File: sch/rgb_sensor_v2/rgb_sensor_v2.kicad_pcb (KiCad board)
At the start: 2 copper layers, 57 parts, among them J1 Conn_01x20_Male, Q1 2N7002, Q2 2N7002, Q3 2N7002, Q4 2N7002, Q5 2N7002, U1 TCS34725FN, U2 TCS34725FN, U3 TCS34725FN, U4 TCS34725FN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

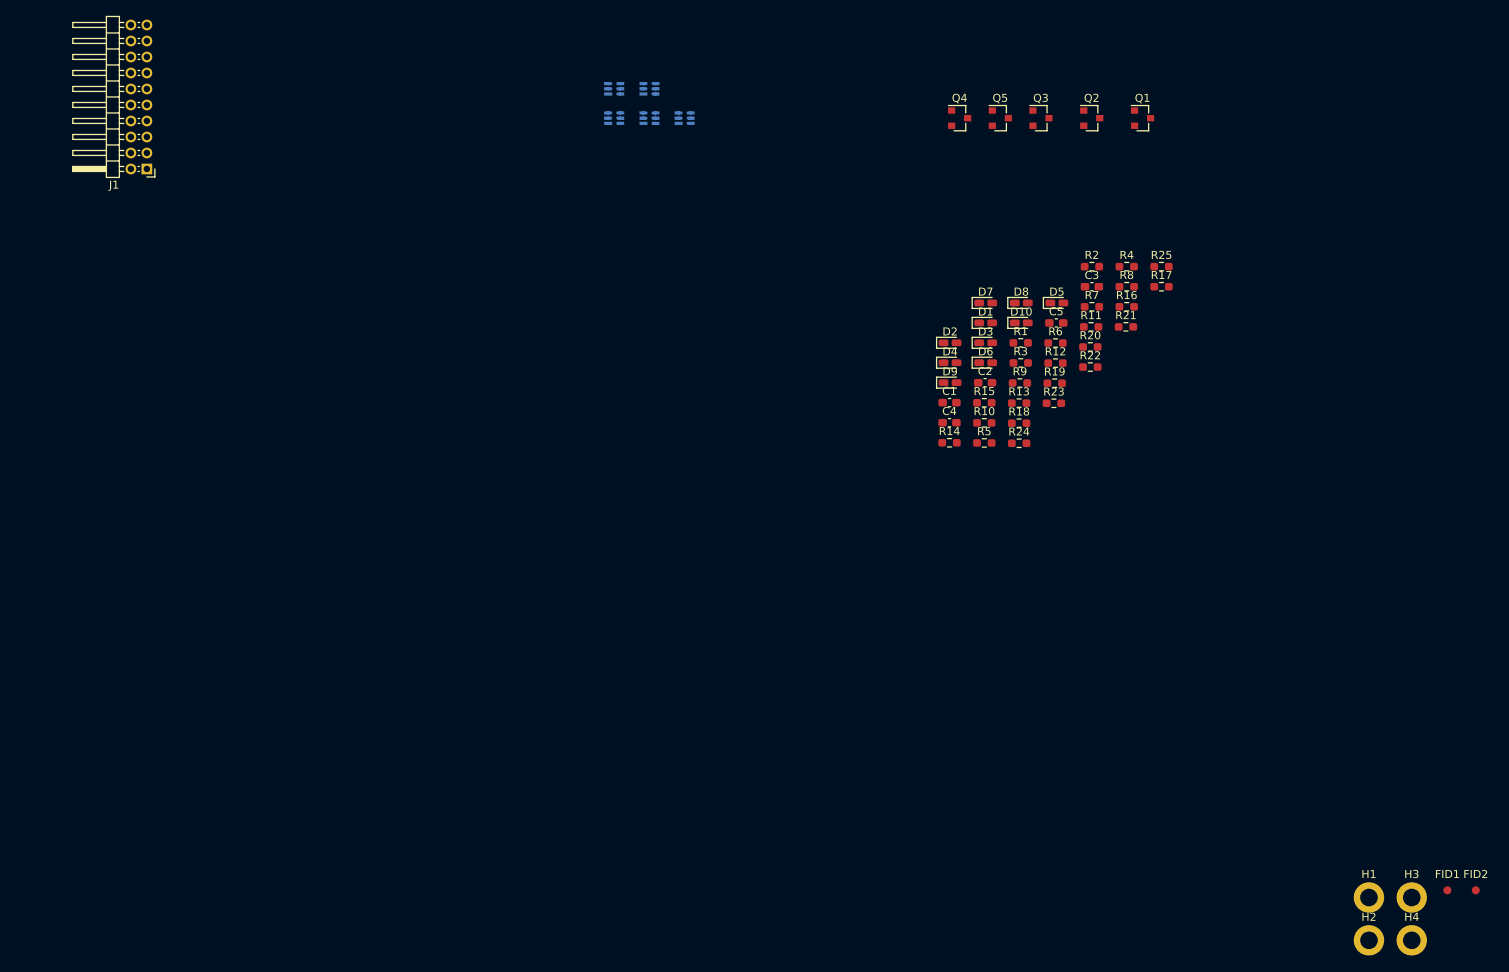
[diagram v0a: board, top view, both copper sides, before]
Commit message: some layout done
beefore changing pin assignment on main connector
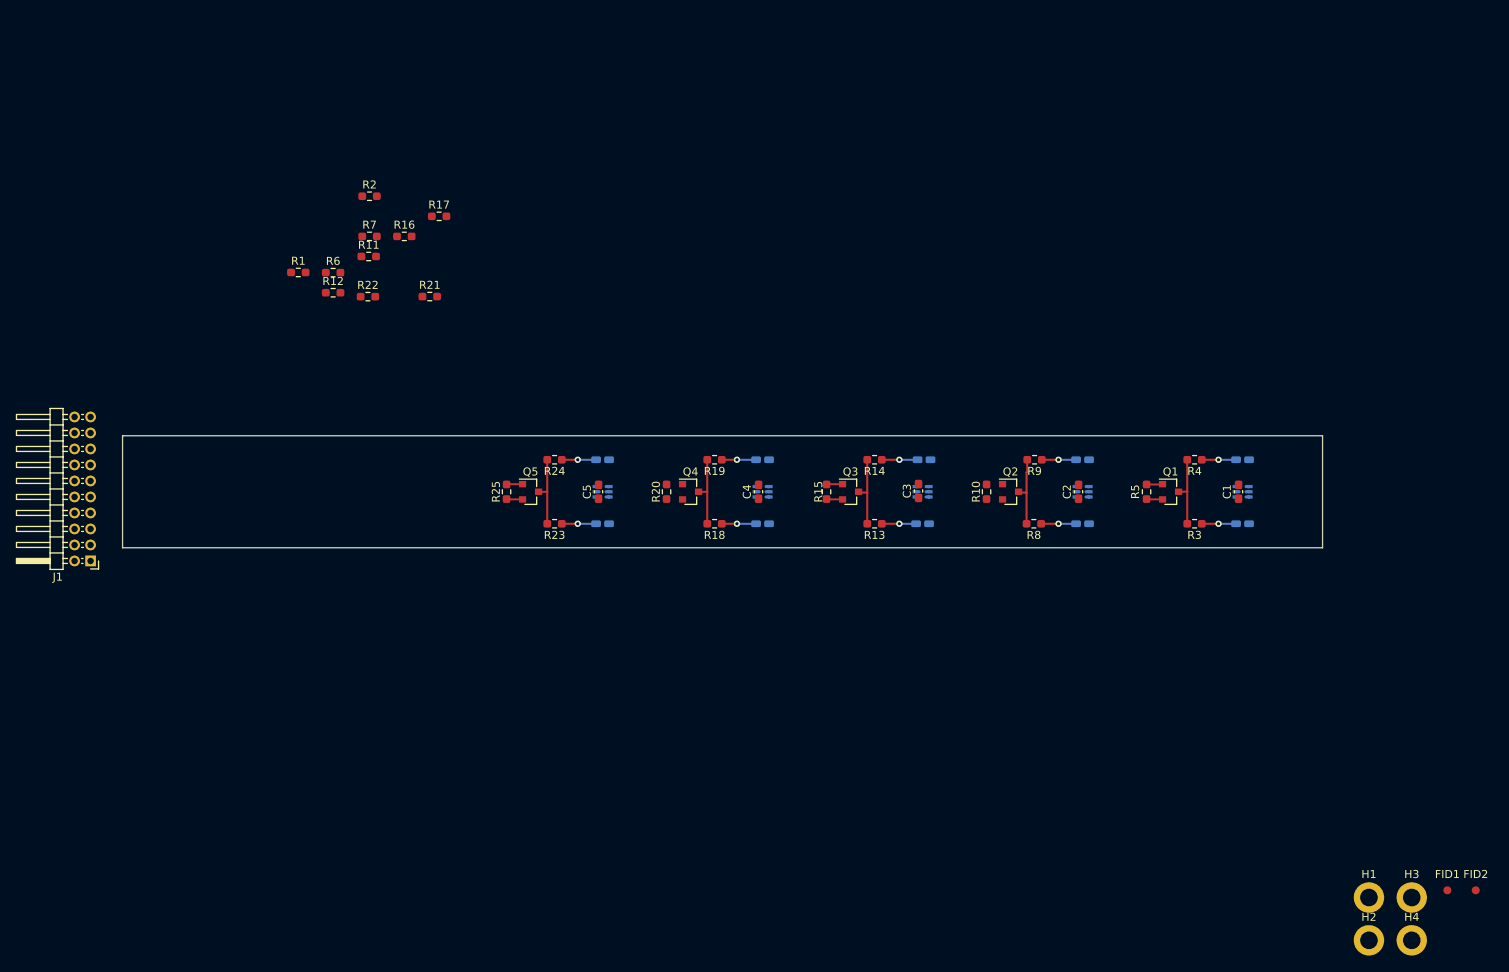
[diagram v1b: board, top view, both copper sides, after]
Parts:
- D1, D10, D2, D3, D4, D5, D6, D7, D8, D9: moved to B.Cu
- moved U1 91.4 mm to (228.4, 97.5)
- moved R12 90.7 mm to (114.7, 72.6)
- moved R17 90.7 mm to (128.0, 63.1)
- moved R22 90.7 mm to (119.1, 73.1)
- moved R6 90.7 mm to (114.7, 70.1)
- moved R11 90.7 mm to (119.2, 68.1)
- moved R2 90.7 mm to (119.3, 60.6)
- moved R7 90.7 mm to (119.3, 65.6)
- moved R1 90.7 mm to (110.4, 70.1)
- moved R16 90.7 mm to (123.6, 65.6)
- moved R21 87.1 mm to (126.8, 73.1)
- moved R25 86.6 mm to (136.4, 97.5), turned to 270 degrees
- moved U2 77.2 mm to (208.4, 97.5)
- moved Q5 75.0 mm to (139.4, 97.5)
- moved R23 64.2 mm to (142.4, 101.5), turned to 180 degrees
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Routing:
- net Net-(Q3-Pad3): track 0.00 -> 9.13 mm
- net Net-(Q5-Pad3): track 0.00 -> 9.09 mm
- net Net-(Q4-Pad3): track 0.00 -> 9.09 mm
- net Net-(Q1-Pad3): track 0.00 -> 9.09 mm
- net Net-(Q2-Pad3): track 0.00 -> 9.08 mm
- net GND: track 0.00 -> 6.05 mm
- net Net-(D6-Pad1): track 0.00 -> 4.46 mm, vias 0 -> 1
- net Net-(D3-Pad1): track 0.00 -> 4.36 mm, vias 0 -> 1
- net Net-(D9-Pad1): track 0.00 -> 4.28 mm, vias 0 -> 1
- net Net-(D8-Pad1): track 0.00 -> 4.28 mm, vias 0 -> 1
- net Net-(D7-Pad1): track 0.00 -> 4.28 mm, vias 0 -> 1
- net Net-(D5-Pad1): track 0.00 -> 4.28 mm, vias 0 -> 1
- net Net-(D4-Pad1): track 0.00 -> 4.28 mm, vias 0 -> 1
- net Net-(D2-Pad1): track 0.00 -> 4.28 mm, vias 0 -> 1
- net Net-(D10-Pad1): track 0.00 -> 4.28 mm, vias 0 -> 1
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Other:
- board outline added: 150 x 14 mm
- board text added: "Desk"

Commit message: zrobiony routing ścieżek
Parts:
- moved H1 54.9 mm to (234.9, 94.1)
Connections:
- J1 pad 10: SDA3 -> SDA2
- J1 pad 11: LED3 -> LED2
- J1 pad 12: SCL4 -> SCL3
- J1 pad 13: SDA4 -> SDA3
- J1 pad 14: LED4 -> LED3
- J1 pad 15: SCL5 -> SCL4
- J1 pad 16: SDA5 -> SDA4
- J1 pad 17: LED5 -> LED4
- J1 pad 18: GND -> SCL5
- J1 pad 19: GND -> SDA5
- J1 pad 20: GND -> LED5
- J1 pad 3: SCL1 -> GND
- J1 pad 4: SDA1 -> GND
- J1 pad 5: LED1 -> GND
- J1 pad 6: SCL2 -> SCL1
- J1 pad 7: SDA2 -> SDA1
- J1 pad 8: LED2 -> LED1
- J1 pad 9: SCL3 -> SCL2
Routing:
- net +3V3: track 0.00 -> 152.3 mm, vias 0 -> 5
- net SDA1: track 0.00 -> 137.0 mm
- net SCL1: track 0.00 -> 131.8 mm
- net LED1: track 2.02 -> 120.2 mm, vias 0 -> 1
- net SDA2: track 0.00 -> 116.0 mm
- net SCL2: track 0.00 -> 111.4 mm
- net LED2: track 0.00 -> 100.5 mm, vias 0 -> 1
- net SDA3: track 0.00 -> 95.0 mm
- net SCL3: track 0.00 -> 88.5 mm
- net SDA4: track 0.00 -> 74.9 mm
- net LED3: track 2.02 -> 76.8 mm, vias 0 -> 1
- net SCL4: track 0.00 -> 67.8 mm
- net LED4: track 0.00 -> 61.4 mm, vias 0 -> 1
- net SDA5: track 0.00 -> 51.3 mm
- net SCL5: track 0.00 -> 45.4 mm
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
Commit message: Zapisany postęp godzinowy
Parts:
- moved R1 116.5 mm to (223.6, 97.5), turned to 90 degrees
- moved R2 112.1 mm to (225.1, 97.5), turned to 90 degrees
- moved R6 93.1 mm to (203.7, 97.5), turned to 90 degrees
- moved R7 91.7 mm to (205.2, 97.5), turned to 90 degrees
- moved R12 65.7 mm to (180.1, 78.9)
- moved R11 61.3 mm to (180.0, 75.8)
- moved H2 52.8 mm to (235.4, 101.5)
- moved J1 4.05 mm to (88.4, 105.5)
- moved H1 0.78 mm to (235.4, 93.5)
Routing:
- net +3V3: track 152.3 -> 230.1 mm, vias 5 -> 13
- net SDA2: track 116.0 -> 118.8 mm, vias 0 -> 1
- net SDA1: track 137.0 -> 139.5 mm, vias 0 -> 1
- net SCL1: track 131.8 -> 133.7 mm, vias 0 -> 1
- net SCL2: track 111.4 -> 113.1 mm, vias 0 -> 1
- added copper zone on F.Cu, net GND

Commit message: Pullus routed
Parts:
- moved R16 51.5 mm to (164.0, 97.5), turned to 90 degrees
- moved R17 50.9 mm to (165.5, 97.5), turned to 90 degrees
- moved R22 35.8 mm to (145.3, 97.5), turned to 90 degrees
- moved R21 29.7 mm to (143.8, 97.5), turned to 90 degrees
- moved R11 22.0 mm to (183.7, 97.5), turned to 90 degrees
- moved R12 19.3 mm to (185.2, 97.5), turned to 90 degrees
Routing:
- net +3V3: track 230.1 -> 239.5 mm
- net SDA5: track 51.3 -> 57.8 mm, vias 0 -> 1
- net SDA3: track 95.0 -> 97.8 mm, vias 0 -> 1
- net SDA4: track 74.9 -> 76.5 mm, vias 0 -> 1
- net SCL4: track 67.8 -> 69.4 mm, vias 0 -> 1
- net SCL3: track 88.5 -> 90.1 mm, vias 0 -> 1
- net SCL5: track 45.4 -> 46.7 mm, vias 0 -> 1

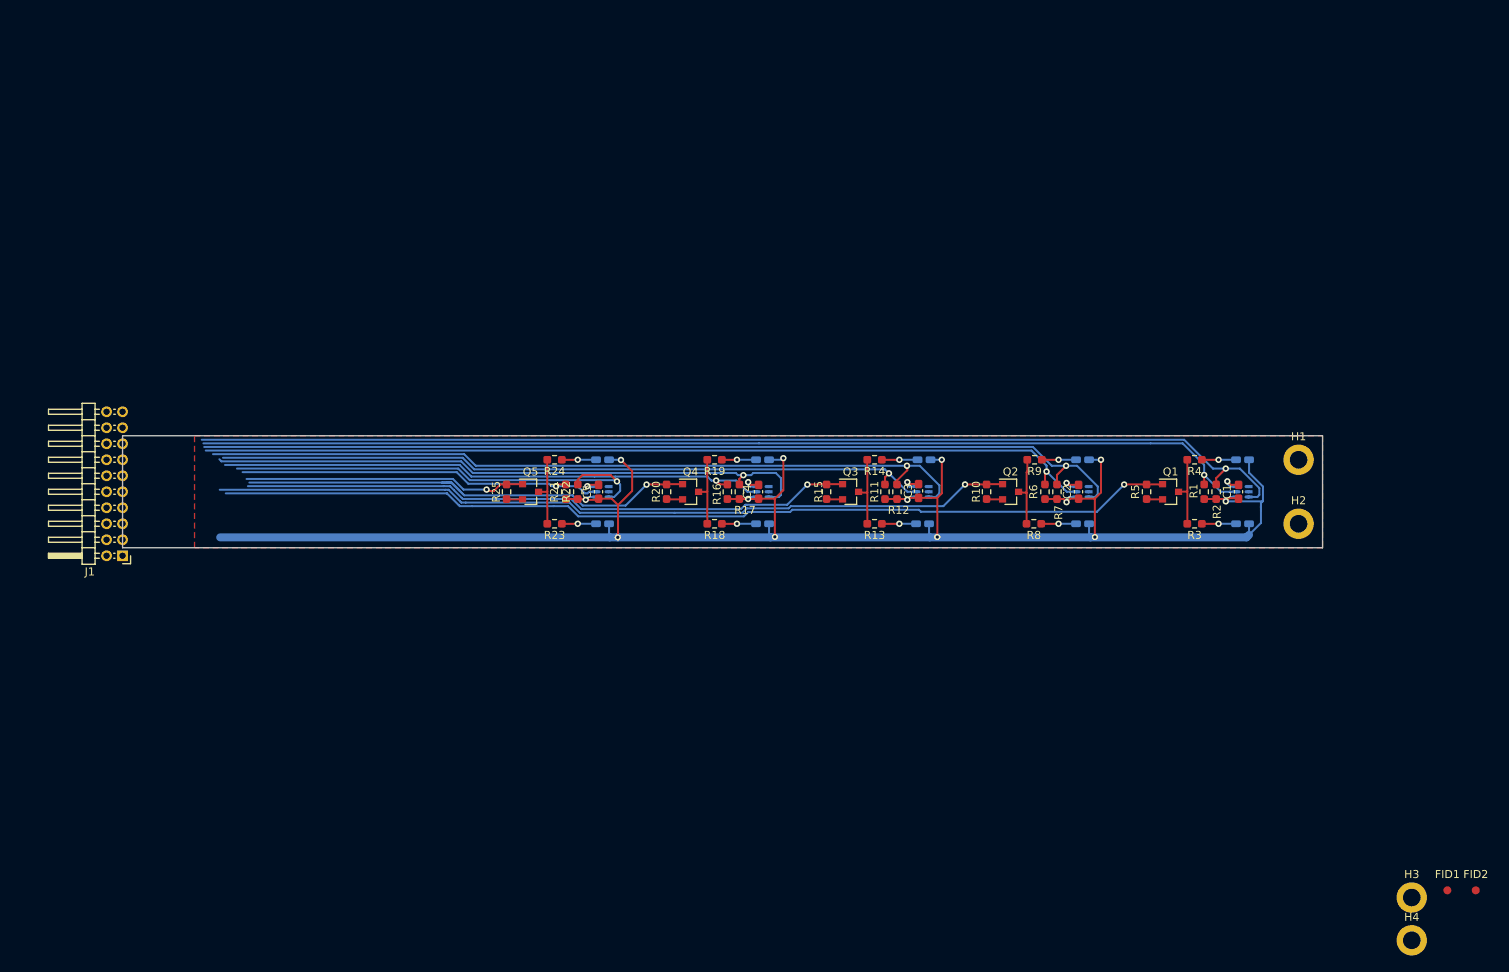
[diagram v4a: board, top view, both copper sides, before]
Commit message: add fab outputs but those are not gerber
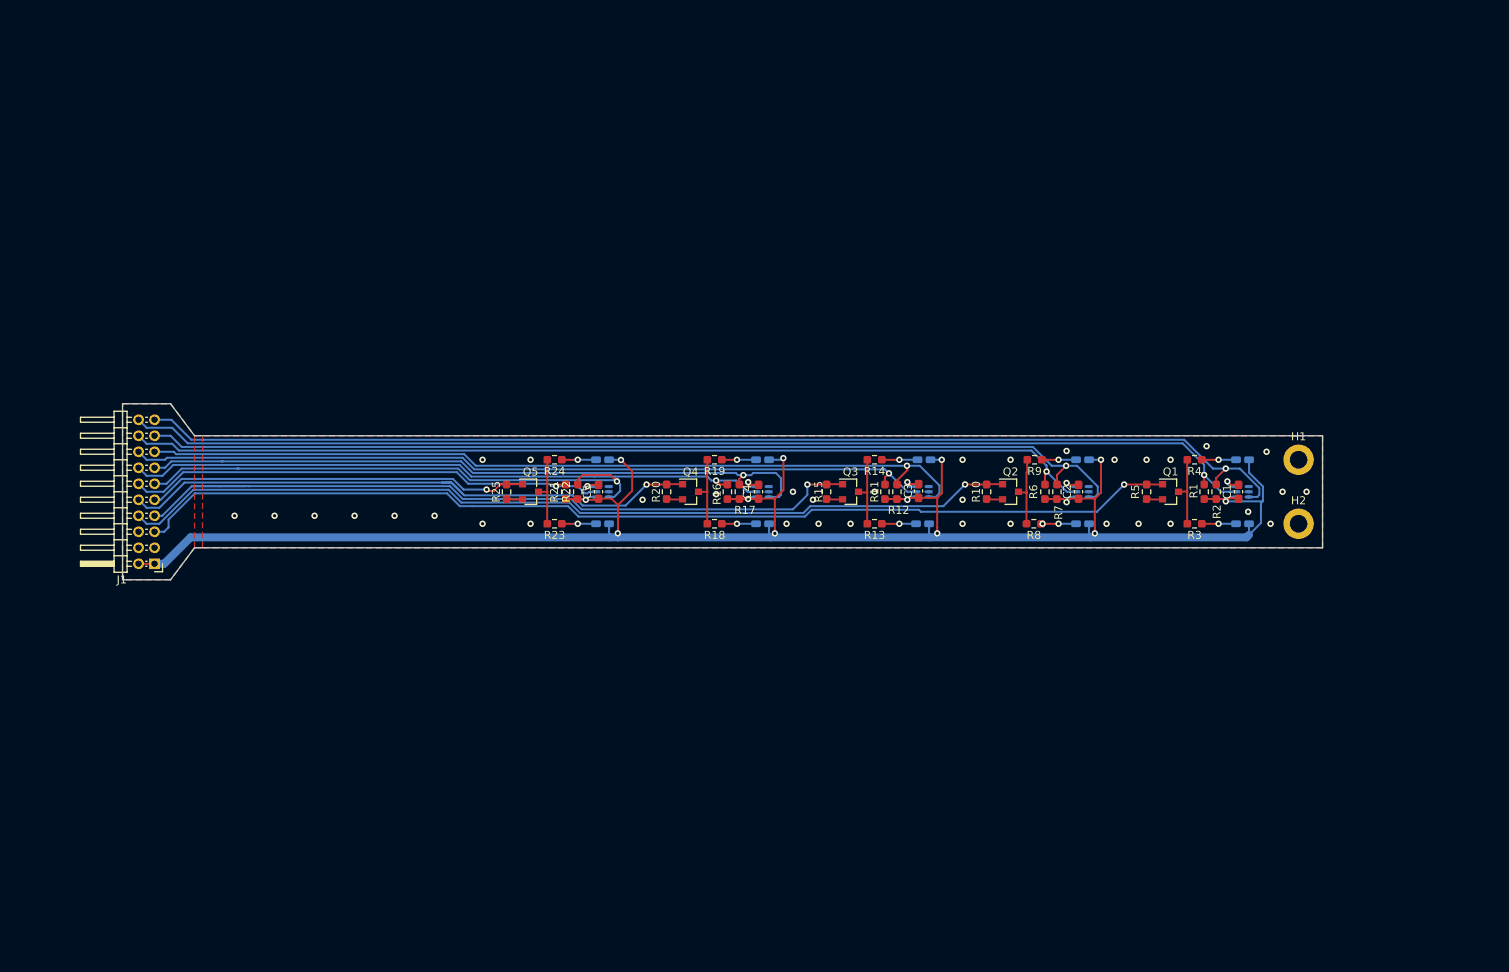
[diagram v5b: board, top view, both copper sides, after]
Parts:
- removed FID1, FID2: Fiducial, Fiducial:Fiducial_1mm_Mask2mm
- removed H3, H4: MountingHole, MountingHole:MountingHole_2.2mm_M2_DIN965_Pad
- moved J1 4.12 mm to (92.4, 106.5)
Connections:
- J1 pad 10: SDA2 -> LED4
- J1 pad 11: LED2 -> SDA5
- J1 pad 12: SCL3 -> SCL5
- J1 pad 13: SDA3 -> SDA4
- J1 pad 14: LED3 -> SCL4
- J1 pad 15: SCL4 -> SDA3
- J1 pad 16: SDA4 -> SCL3
- J1 pad 17: LED4 -> SDA2
- J1 pad 18: SCL5 -> SCL2
- J1 pad 19: SDA5 -> SDA1
- J1 pad 20: LED5 -> SCL1
- J1 pad 5: GND -> LED1
- J1 pad 6: SCL1 -> GND
- J1 pad 7: SDA1 -> LED3
- J1 pad 8: LED1 -> LED2
- J1 pad 9: SCL2 -> LED5
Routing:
- net LED3: track 76.8 -> 98.0 mm
- net LED4: track 61.4 -> 77.0 mm
- net SCL5: track 46.7 -> 61.1 mm
- net LED5: track 35.5 -> 48.1 mm
- net LED2: track 100.5 -> 112.9 mm
- net SCL4: track 69.4 -> 81.5 mm
- net LED1: track 120.2 -> 131.6 mm
- net SDA5: track 57.8 -> 69.1 mm
- net SCL3: track 90.1 -> 101.1 mm
- net SCL1: track 133.7 -> 143.1 mm
- net SCL2: track 113.1 -> 122.3 mm
- net +3V3: track 239.5 -> 248.7 mm
- net SDA4: track 76.5 -> 85.0 mm
- net SDA3: track 97.8 -> 105.3 mm
- net SDA1: track 139.5 -> 146.6 mm
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- added copper zone on B.Cu, net GND
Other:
- board size 150 x 14 mm -> 150 x 22 mm

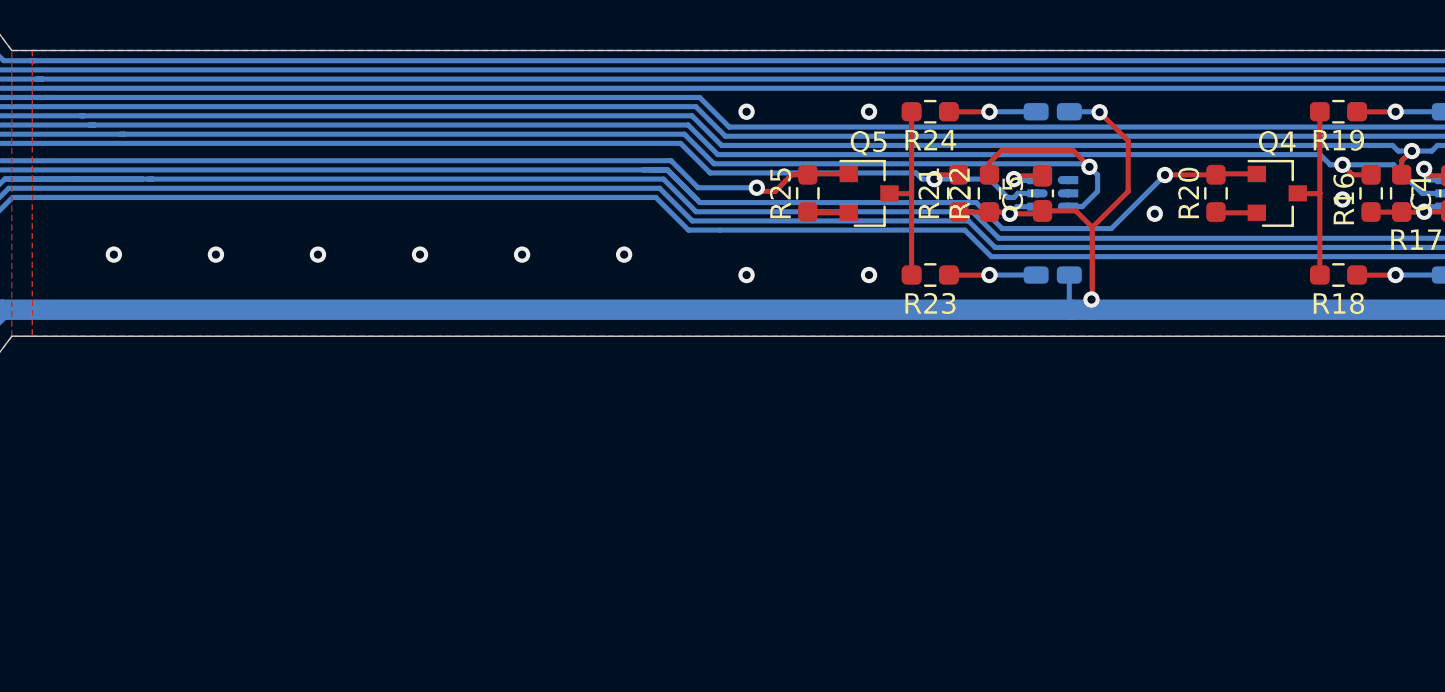
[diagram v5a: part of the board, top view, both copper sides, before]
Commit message: dodana plytka ctrl i zrobiony routing w 90%
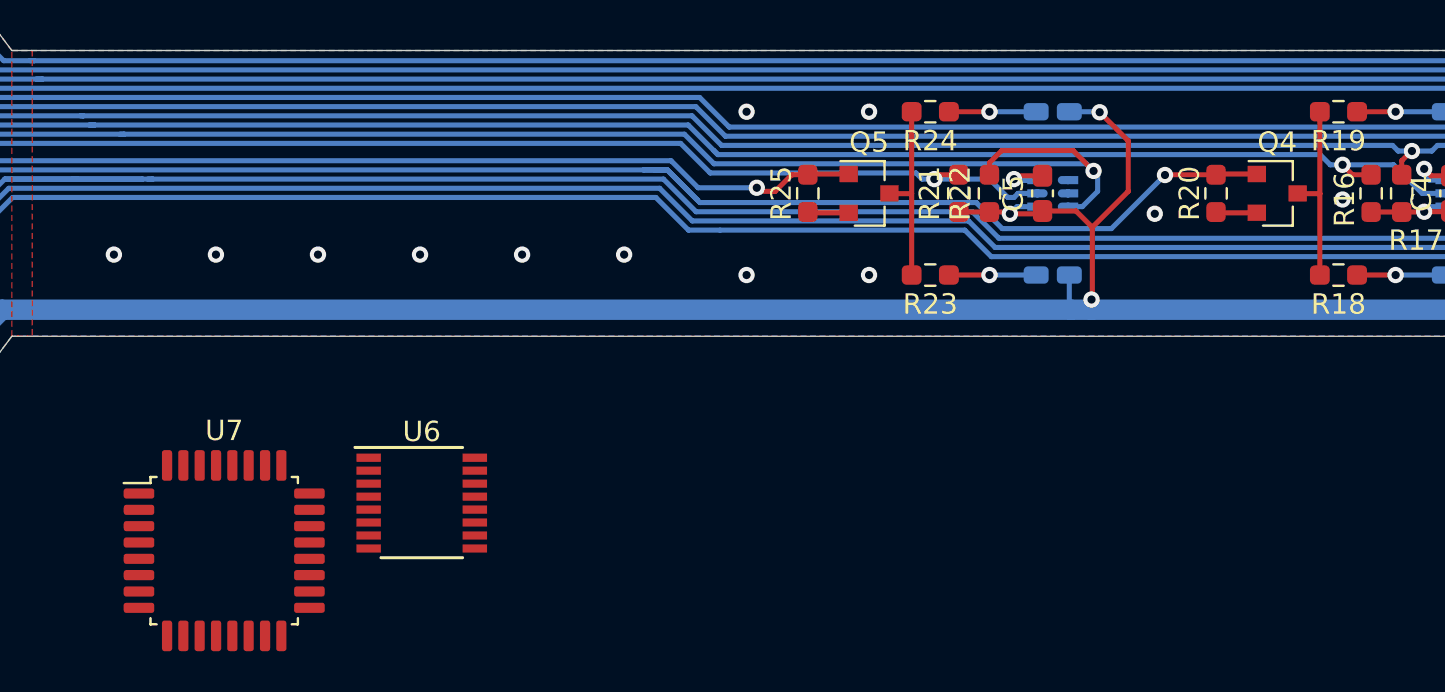
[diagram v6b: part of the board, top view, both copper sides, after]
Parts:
- added U6: FT230XS, Package_SO:SSOP-16_3.9x4.9mm_P0.635mm, F.Cu at (117.5, 112.7)
- added U7: STM32F030K6Tx, Package_QFP:LQFP-32_7x7mm_P0.8mm, F.Cu at (107.8, 115.0)

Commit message: add gerber files
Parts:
- removed U6: FT230XS, Package_SO:SSOP-16_3.9x4.9mm_P0.635mm
- removed U7: STM32F030K6Tx, Package_QFP:LQFP-32_7x7mm_P0.8mm
- J1: footprint Connector_PinHeader_2.00mm:PinHeader_2x10_P2.00mm_Horizontal -> Connector_JST:JST_PHD_S20B-PHDSS_2x10_P2.00mm_Horizontal; moved to B.Cu
- turned J1 to 90 degrees
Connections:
- U1 pad 4: Net-(U1-Pad4) -> (no net)
- U1 pad 5: Net-(U1-Pad5) -> (no net)
- U2 pad 4: Net-(U2-Pad4) -> (no net)
- U2 pad 5: Net-(U2-Pad5) -> (no net)
- U3 pad 4: Net-(U3-Pad4) -> (no net)
- U3 pad 5: Net-(U3-Pad5) -> (no net)
- U4 pad 4: Net-(U4-Pad4) -> (no net)
- U4 pad 5: Net-(U4-Pad5) -> (no net)
- U5 pad 4: Net-(U5-Pad4) -> (no net)
- U5 pad 5: Net-(U5-Pad5) -> (no net)
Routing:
- net GND: vias 41 -> 54
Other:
- board text added: "2020"
- board text added: "kelectronics.pl"
